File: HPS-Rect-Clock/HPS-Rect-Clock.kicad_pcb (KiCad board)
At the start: 2 copper layers, 140 x 90 mm, 52 parts, among them J1 Conn_01x06, J2 Power_inlet_vertical, SW1 Omron_B3F_SPST, SW2 Omron_B3F_SPST, SW3 Omron_B3F_SPST, SW4 Omron_B3F_SPST, SW5 Omron_B3F_SPST, U1 DS1307_DIP-8, U2 ATmega328-PU, U3 L7805, Y1 Crystal_16MHz, Y2 Crystal_32768Hz

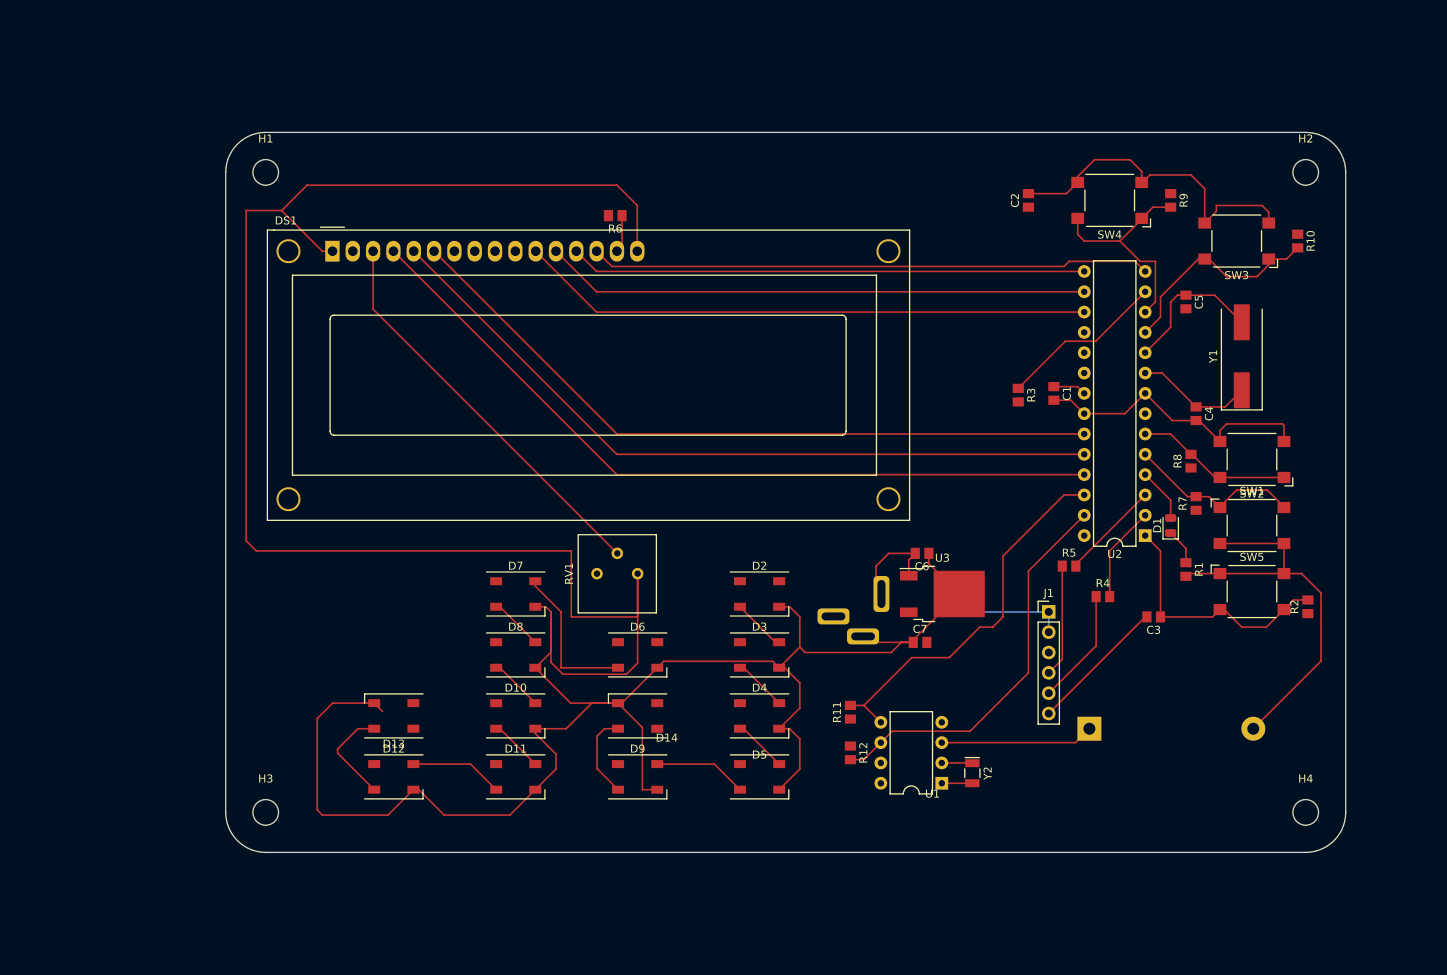
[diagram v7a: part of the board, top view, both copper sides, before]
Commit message: only gnd left
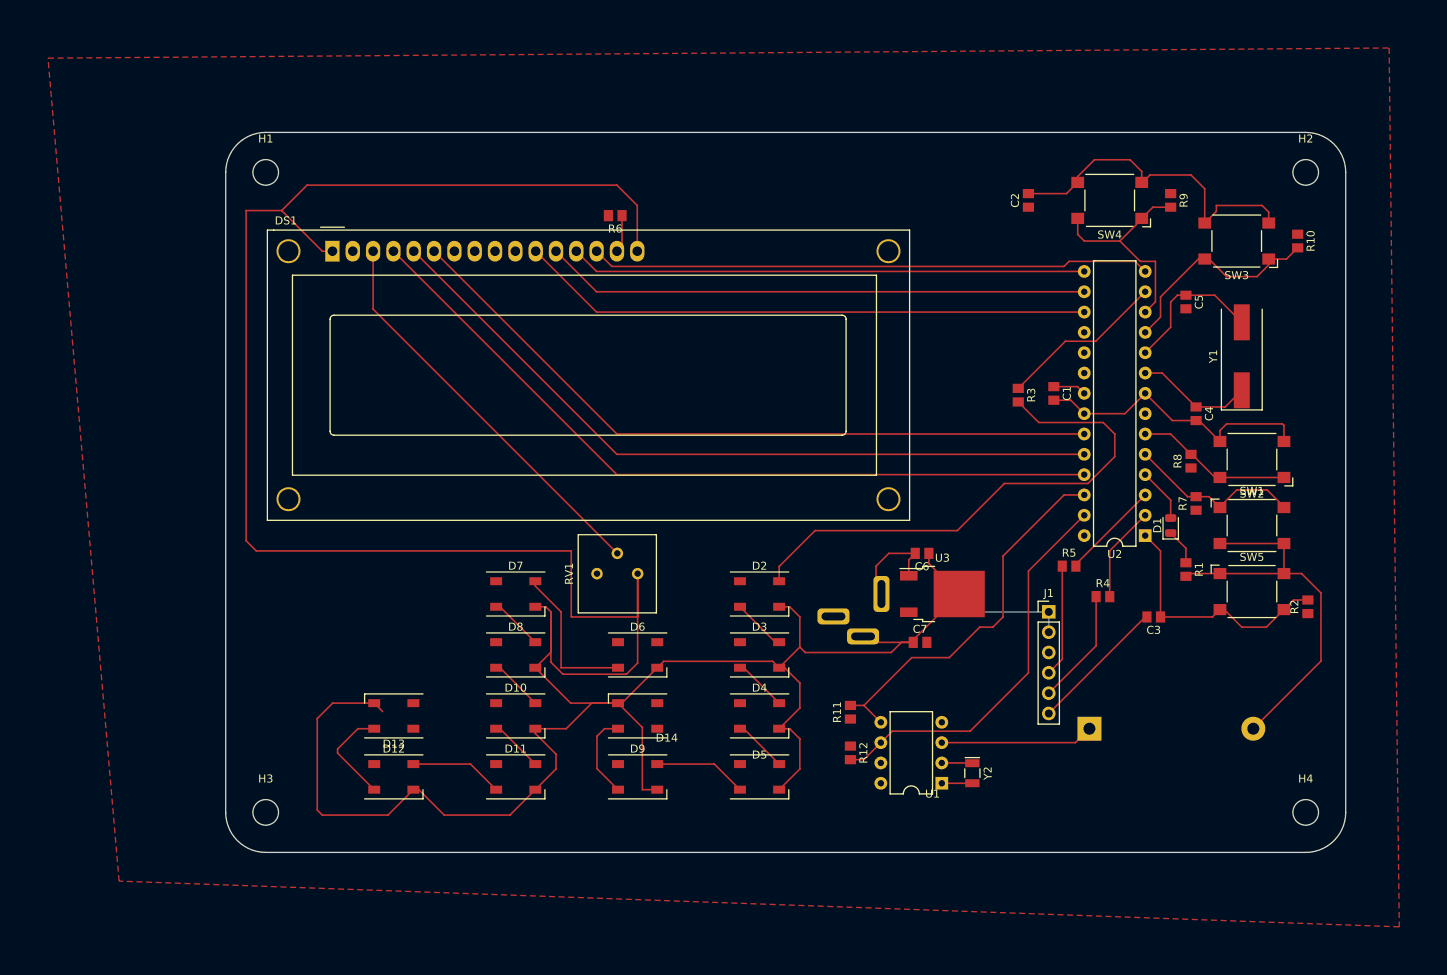
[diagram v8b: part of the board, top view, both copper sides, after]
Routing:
- net NEO: track 0.00 -> 66.0 mm
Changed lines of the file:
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@@
   (segment (start 198.12 100.965) (end 198.12 103.2025) (width 0.2032) (layer "F.Cu") (net 11))
   (segment (start 194.935 97.78) (end 198.12 100.965) (width 0.2032) (layer "F.Cu") (net 11))
+  (segment (start 171.45 104.775) (end 177.3402 98.8848) (width 0.2032) (layer "F.Cu") (net 12))
+  (segment (start 153.67 104.775) (end 171.45 104.775) (width 0.2032) (layer "F.Cu") (net 12))
+  (segment (start 191.135 92.71) (end 189.6898 91.2648) (width 0.2032) (layer "F.Cu") (net 12))
+  (segment (start 189.6898 91.2648) (end 181.6398 91.2648) (width 0.2032) (layer "F.Cu") (net 12))
+  (segment (start 181.6398 91.2648) (end 179.07 88.695) (width 0.2032) (layer "F.Cu") (net 12))
+  (segment (start 149.18 111.1) (end 149.18 109.265) (width 0.2032) (layer "F.Cu") (net 12))
+  (segment (start 191.135 95.522424) (end 191.135 92.71) (width 0.2032) (layer "F.Cu") (net 12))
+  (segment (start 177.3402 98.8848) (end 187.772624 98.8848) (width 0.2032) (layer "F.Cu") (net 12))
+  (segment (start 187.772624 98.8848) (end 191.135 95.522424) (width 0.2032) (layer "F.Cu") (net 12))
+  (segment (start 149.18 109.265) (end 153.67 104.775) (width 0.2032) (layer "F.Cu") (net 12))
   (segment (start 148.7 118.72) (end 149.18 118.72) (width 0.2032) (layer "F.Cu") (net 13))
   (segment (start 144.28 114.3) (end 148.7 118.72) (width 0.2032) (layer "F.Cu") (net 13))
@@
       )
     )
+  )
+  (zone (net 4) (net_name "VCC") (layer "F.Cu") (hatch edge 0.508)
+    (connect_pads (clearance 0))
+    (min_thickness 0.254)
+    (fill (thermal_gap 0.3048) (thermal_bridge_width 0.508))
+    (polygon
+      (pts
+        (xy 226.695 154.305)
+        (xy 66.675 148.59)
+        (xy 57.785 45.72)
+        (xy 225.425 44.45)
+      )
+    )
